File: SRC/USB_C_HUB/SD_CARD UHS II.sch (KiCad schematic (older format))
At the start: 20 parts

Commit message: ALL DONE BUT THE HDMI SECTION. NEED FOOTPRINT ASSIGNMENT
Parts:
- removed C? (x2): 18pF, symbol Device:C_Small
- removed C?: 1uF_1%_0.1ohm, symbol Device:C_Small
- removed C?: 1uF, symbol Device:C_Small
- removed C? (x2): 0.1uF, symbol Device:C_Small
- removed C?: 4.7uF, symbol Device:C_Small
- removed C?: 1nF, symbol Device:C_Small
- removed R?: 1M, symbol Device:R_US
- removed R?: 100K, symbol Device:R_US
- removed R?: 12K_1%, symbol Device:R_US
- removed R? (x2): 10K, symbol Device:R_US
- added C164, C165: 18pF, symbol Device:C_Small
- added C166: 1uF_1%_0.1ohm, symbol Device:C_Small
- added C167: 1uF, symbol Device:C_Small
- added C169, C170: 0.1uF, symbol Device:C_Small
- added C174: 4.7uF, symbol Device:C_Small
- added C175: 1nF, symbol Device:C_Small
- added R94: 1M, symbol Device:R_US
- added R95: 100K, symbol Device:R_US
- added R96: 12K_1%, symbol Device:R_US
- added R97, R98: 10K, symbol Device:R_US
- IC6: renamed from IC?; footprint QFN50P600X600X100-37N-D -> SamacSys_Parts_2:QFN50P600X600X100-37N-D
- gave numbers to parts that had none: 6
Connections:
- net +3V3: now also C169.1, C170.1, R95.1
- net CRD_PWR: now also C174.1, C175.1, R98.2
- net GND: now also C164.2, C165.2, C166.2, C167.2, C169.2, C170.2, C174.2, C175.2, R96.2, R97.1, R98.1
- net XTAL1: now also C165.1, R94.1
- net XTAL2: now also C164.1, R94.2
- net at IC6.18 (RESET_N): now also R95.2
- net at IC6.34 (VDD18PLL): now also C166.1
- net at IC6.13 (VDD18): now also C167.1
- net at IC6.35 (RBIAS): now also R96.1
- net at IC6.29 (GPIO4): now also R97.2

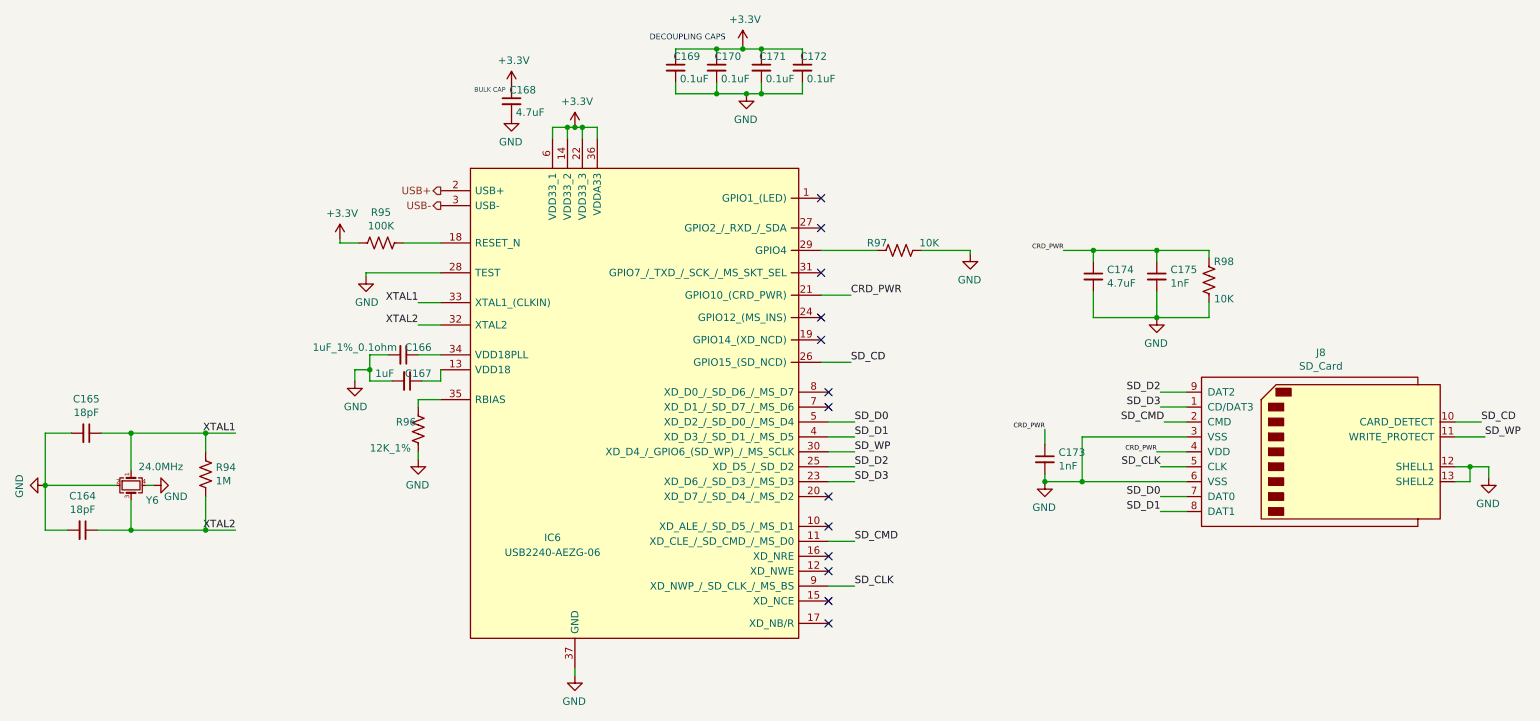
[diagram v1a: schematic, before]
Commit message: schematic capture complete. Pending Footprint assignment. accetable Errors=21
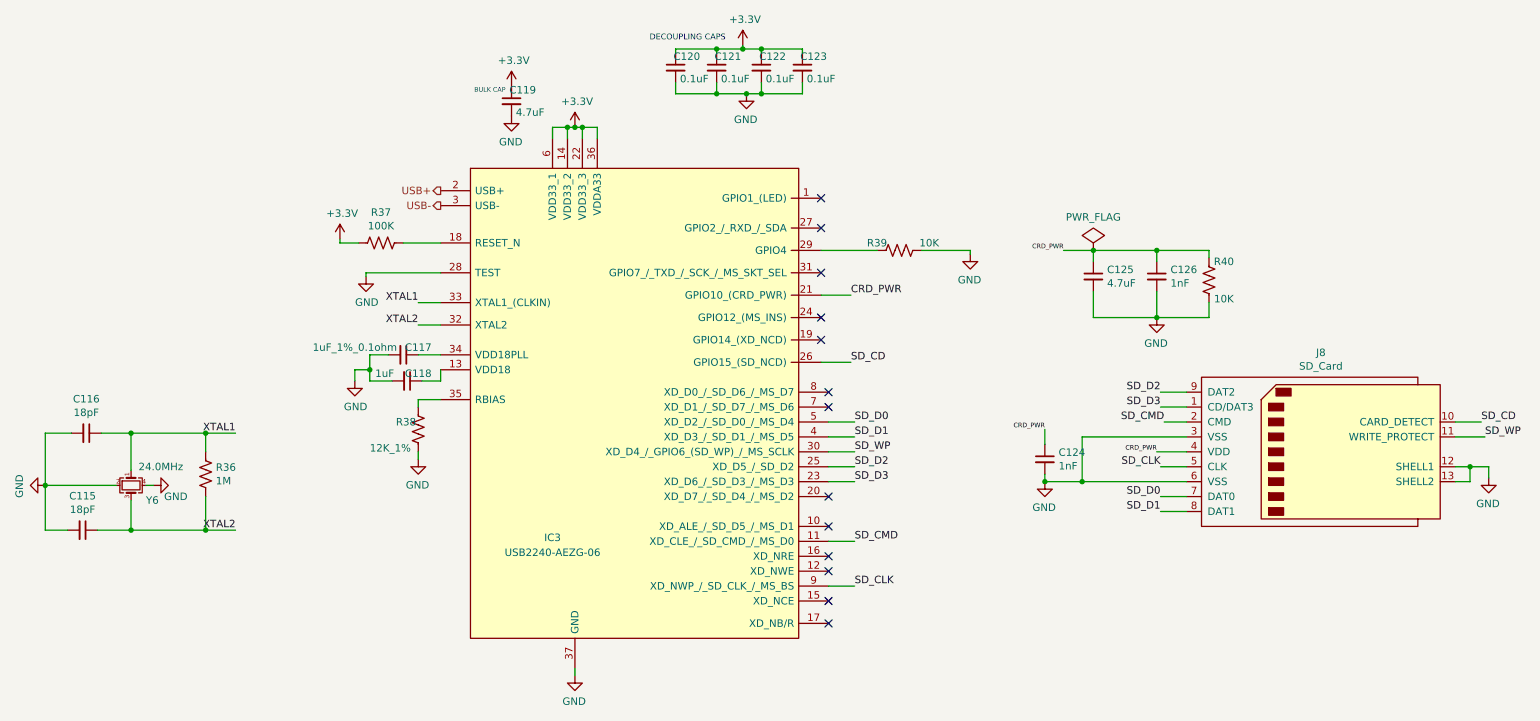
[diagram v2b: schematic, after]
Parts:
- renumbered C164 to C115, C165 to C116, C166 to C117, C167 to C118, C168 to C119, C169 to C120, C170 to C121, C171 to C122, C172 to C123, C173 to C124, C174 to C125, C175 to C126, IC6 to IC3, R94 to R36, R95 to R37, R96 to R38, R97 to R39, R98 to R40
